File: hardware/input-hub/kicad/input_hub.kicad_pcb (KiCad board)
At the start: 2 copper layers, 116 x 36 mm, 34 parts, among them J1 ACJMIH, J10 XIAO_BAT_SOLDER_ACCESS, J11 S2B-PH-SM4-TB_LF__SN_, J12 PJ-307, J13 PJ-307, J14 PJ-307, J2 ACJMIH, J3 ACJMIH, J5 54602-908LF, J6 BM04B-SRSS-TB_LF__SN_, J7 Conn_01x04, J8 Conn_01x02, U1 102010448, U2 TPD4E05U06DQAR, U3 TPD4E05U06DQAR

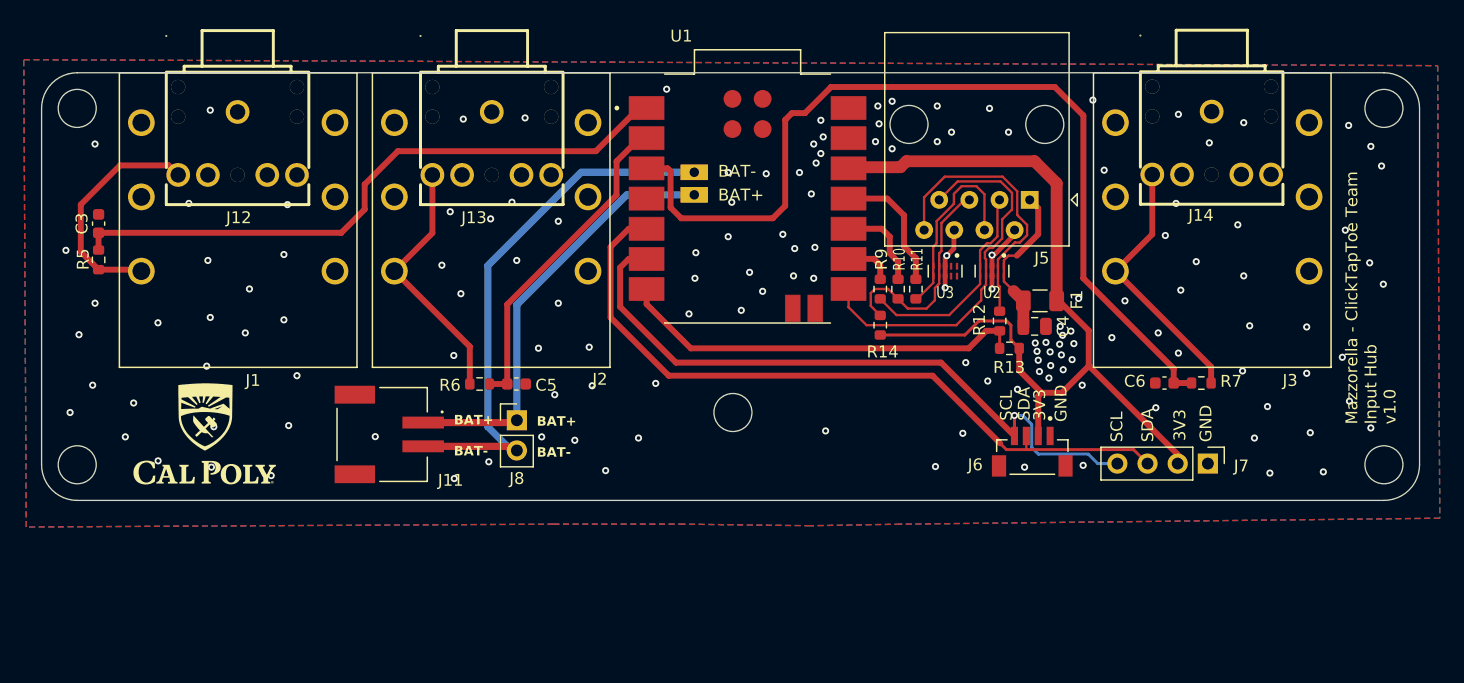
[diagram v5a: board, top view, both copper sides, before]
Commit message: feat: remove third TS jack and make vertical JST battery connector
- Remove the third pedal jack option to reduce board width.
  - Align edge connectors for a cleaner enclosure-facing layout.
  - Replace the horizontal battery JST with a vertical B2B-PH-SM4-TB footprint.
  - Remove stale horizontal JST symbol, footprint, and model assets.
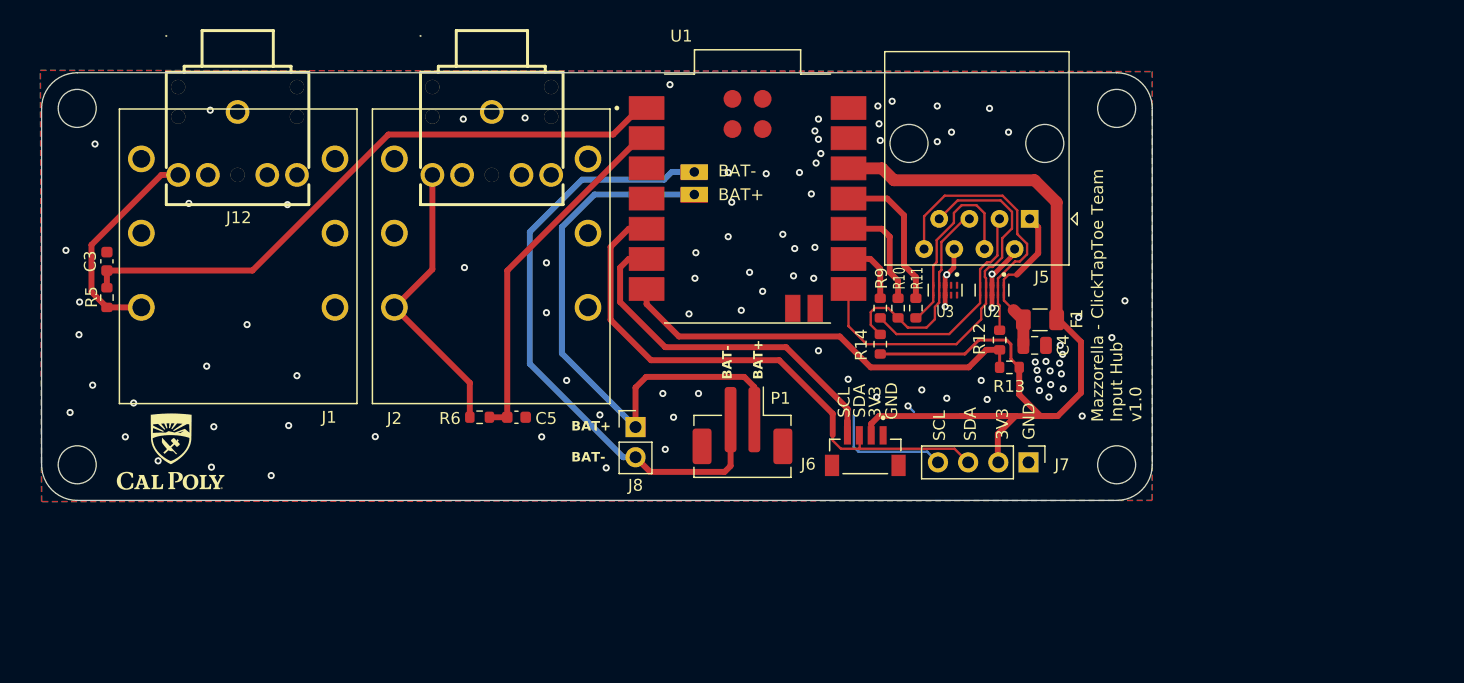
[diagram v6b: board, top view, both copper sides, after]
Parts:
- removed C6: 1u, Capacitor_SMD:C_0603_1608Metric
- removed H5: MountingHole, MountingHole:MountingHole_3.2mm_M3_ISO14580
- removed J10: XIAO_BAT_SOLDER_ACCESS, input_hub:XIAO_BAT_SOLDER_ACCESS
- removed J11: S2B-PH-SM4-TB_LF__SN_, input_hub:JST_S2B-PH-SM4-TB_LF__SN_
- removed J14: PJ-307, input_hub:AUDIO-TH_PJ-307
- removed J3: ACJMIH, input_hub:AMPHENOL_ACJMIH
- removed R7: 330, Resistor_SMD:R_0603_1608Metric
- added J9: XIAO_BAT_SOLDER_ACCESS, input_hub:XIAO_BAT_SOLDER_ACCESS, F.Cu at (151.9, 65.3)
- added P1: B2B-PH-SM4-TB, input_hub:JST_PH_B2B-PH-SM4-TB_1x02-1MP_P2.00mm_Vertical, F.Cu at (156.0, 86.7)
- moved H2 22.5 mm to (187.5, 60.0)
- moved H4 22.5 mm to (187.5, 90.0)
- moved J7 15.1 mm to (180.1, 89.8)
- moved J6 14.1 mm to (166.3, 89.3)
- moved J8 10.0 mm to (147.0, 86.8)
- moved C3 3.25 mm to (102.5, 72.9)
- moved R5 3.25 mm to (102.5, 75.9)
- moved J1 3.05 mm to (113.5, 70.5)
- moved J2 3.05 mm to (134.8, 70.5)
- moved C5 2.80 mm to (137.0, 86.0)
- moved R6 2.80 mm to (133.9, 86.0)
- moved C4 1.60 mm to (180.6, 80.0)
- moved R10 1.60 mm to (169.1, 76.8)
- moved R11 1.60 mm to (170.6, 76.8)
- moved R9 1.60 mm to (167.6, 76.8)
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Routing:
- net Button3: track 77.3 -> 0.00 mm
- net Net-(J14-Pad5): track 22.2 -> 0.00 mm
- net ENC_A: track 61.7 -> 47.3 mm
- net ENC_B: track 56.7 -> 42.9 mm
- net BAT+: track 36.4 -> 48.5 mm
- net +3V3: track 74.1 -> 84.9 mm
- net BAT-: track 45.5 -> 51.8 mm
- net Net-(J13-Pad5): track 21.6 -> 24.5 mm
- net Button2: track 27.4 -> 30.2 mm
- net MOT_RJ45: track 31.8 -> 33.4 mm
- net Net-(U1-D9/MISO): track 7.62 -> 9.22 mm
- net Net-(U1-D10/MOSI): track 11.1 -> 12.7 mm
- net Net-(U1-D8/SCK): track 4.07 -> 5.50 mm
- net Net-(J1-PadT): track 19.6 -> 18.4 mm
- net Net-(U1-D6/TX): track 34.6 -> 35.3 mm
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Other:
- board size 116 x 36 mm -> 93.5 x 36 mm

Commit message: feat: prep input hub for JLC assembly
- Add JLC-oriented board constraints, DRC exclusions, revised vias, and production metadata.
  - Add input hub 3D model links, silkscreen logos, PJ-307 footprint updates, and vertical battery
  JST metadata.
  - Route/document PMW3610 reset and MOTION pull-up support with firmware retry configuration.
  - Clean up remaining EC11 encoder library artifacts and stale encoder nets.
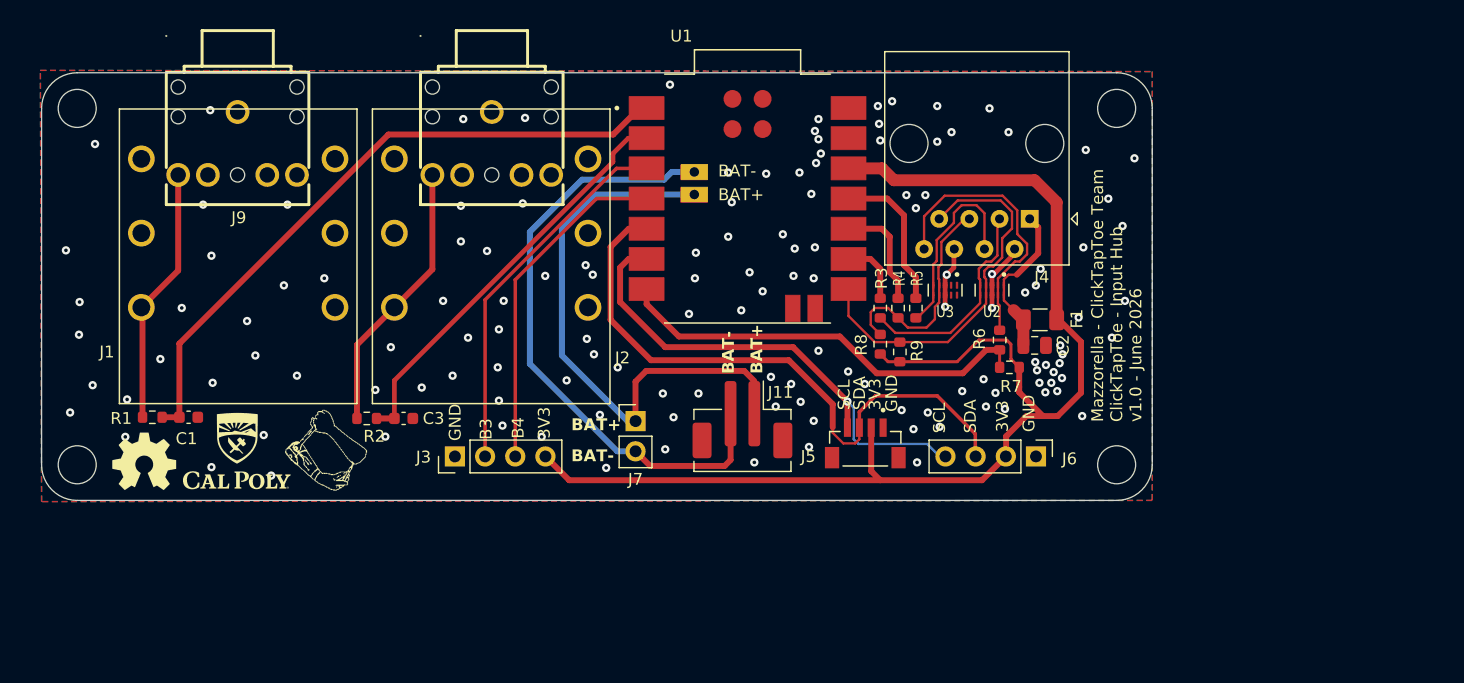
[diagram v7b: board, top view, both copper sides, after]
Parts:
- added G***: EMPOWER_Hand_Line_Silkscreen_7mm_MildSmooth_Mirrored, input_hub:EMPOWER_Hand_Line_Silkscreen_7mm_MildSmooth_Mirrored, F.Cu at (121.0, 88.8)
- added G***: EMPOWER_Hand_Line_Silkscreen_7mm_MildSmooth, input_hub:EMPOWER_Hand_Line_Silkscreen_7mm_MildSmooth, B.Cu at (121.0, 88.8)
- added J3: Conn_01x04, Connector_PinHeader_2.54mm:PinHeader_1x04_P2.54mm_Vertical, F.Cu at (131.8, 89.3)
- added R9: 10k, Resistor_SMD:R_0603_1608Metric, F.Cu at (169.2, 80.5)
- moved C1 14.8 mm to (109.4, 86.0), turned to 180 degrees
- moved R1 10.8 mm to (106.3, 86.0), turned to 180 degrees
- moved C3 9.50 mm to (127.5, 86.1)
- moved R2 9.50 mm to (124.4, 86.1)
- moved J6 0.80 mm to (180.7, 89.3)
- moved J5 0.65 mm to (166.3, 88.7)
- moved J11 0.50 mm to (156.0, 86.2)
- moved J7 0.50 mm to (147.0, 86.3)
- renumbered C3 to C1, C4 to C2, C5 to C3, J13 to J10, P1 to J11, J5 to J4, J6 to J5, J7 to J6, J8 to J7, J9 to J8, J12 to J9, R5 to R1, R6 to R2, R9 to R3, R10 to R4, R11 to R5, R12 to R6, R13 to R7, R14 to R8
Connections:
- net ENC_A renamed SDA
- net ENC_B renamed SCL
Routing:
- net Button3: track 0.00 -> 31.4 mm
- net Button4: track 0.00 -> 28.8 mm
- net +3V3: track 84.9 -> 110.4 mm
- net SDA: track 47.3 -> 52.5 mm
- net Button2: track 30.2 -> 34.8 mm
- net Net-(J1-PadT): track 18.4 -> 21.7 mm
- net Button1: track 52.5 -> 55.2 mm
- net SCL: track 42.9 -> 41.3 mm
- net Net-(J10-Pad5): track 24.5 -> 23.3 mm
- net MOT_RJ45: track 33.4 -> 32.3 mm
- net GND: vias 93 -> 139
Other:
- board text added: "B3"
- board text added: "B4"
- board text added: "Mazzorella - ClickTapToe Team ClickTapToe - Input Hub v1.0 - June 2026"
- board text removed: "Mazzorella - ClickTapToe Team Input Hub v1.0"

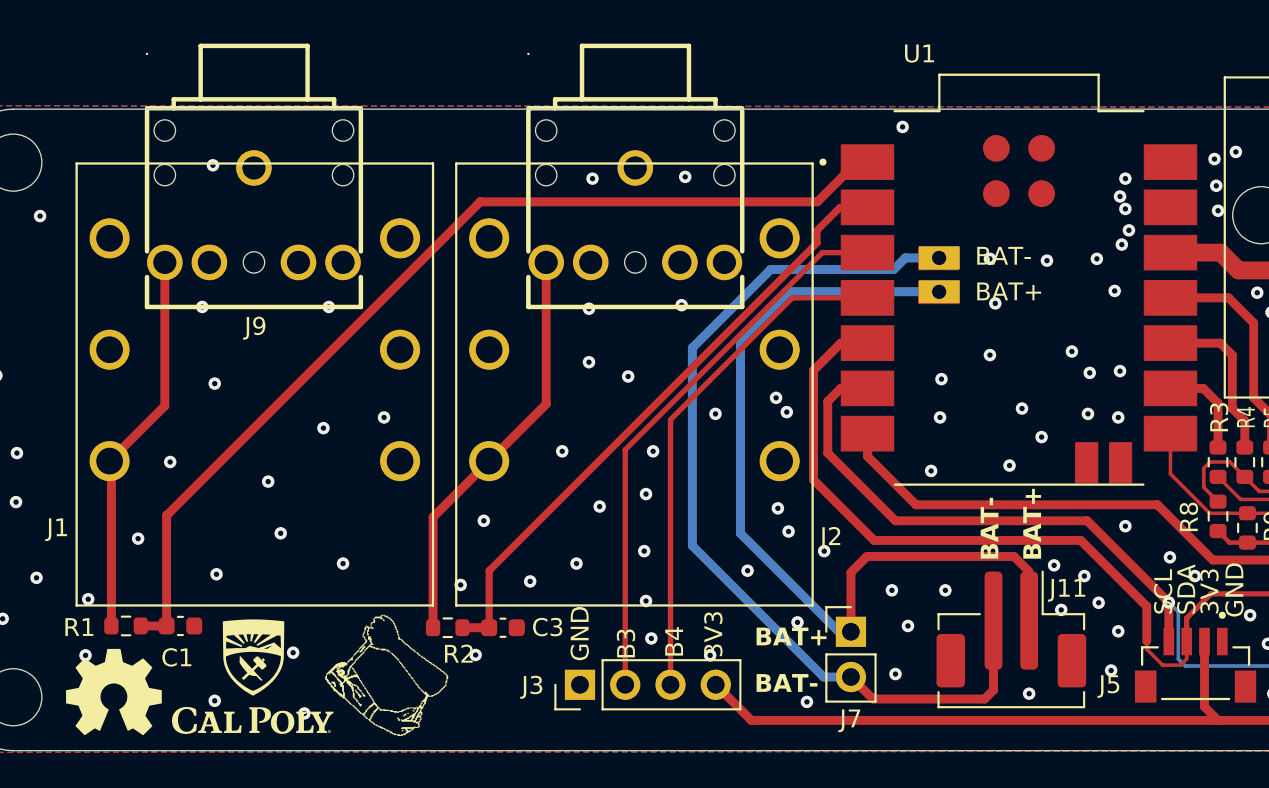
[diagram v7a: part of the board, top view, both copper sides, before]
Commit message: fix: add input hub pedal normal jumpers
- Route pedal jack normal contacts
  through optional 0R jumpers to ground.
  - Use existing 0603 0R jumper sourcing for the new input hub build options.
  - Track release-ready input hub fabrication outputs for ordering.
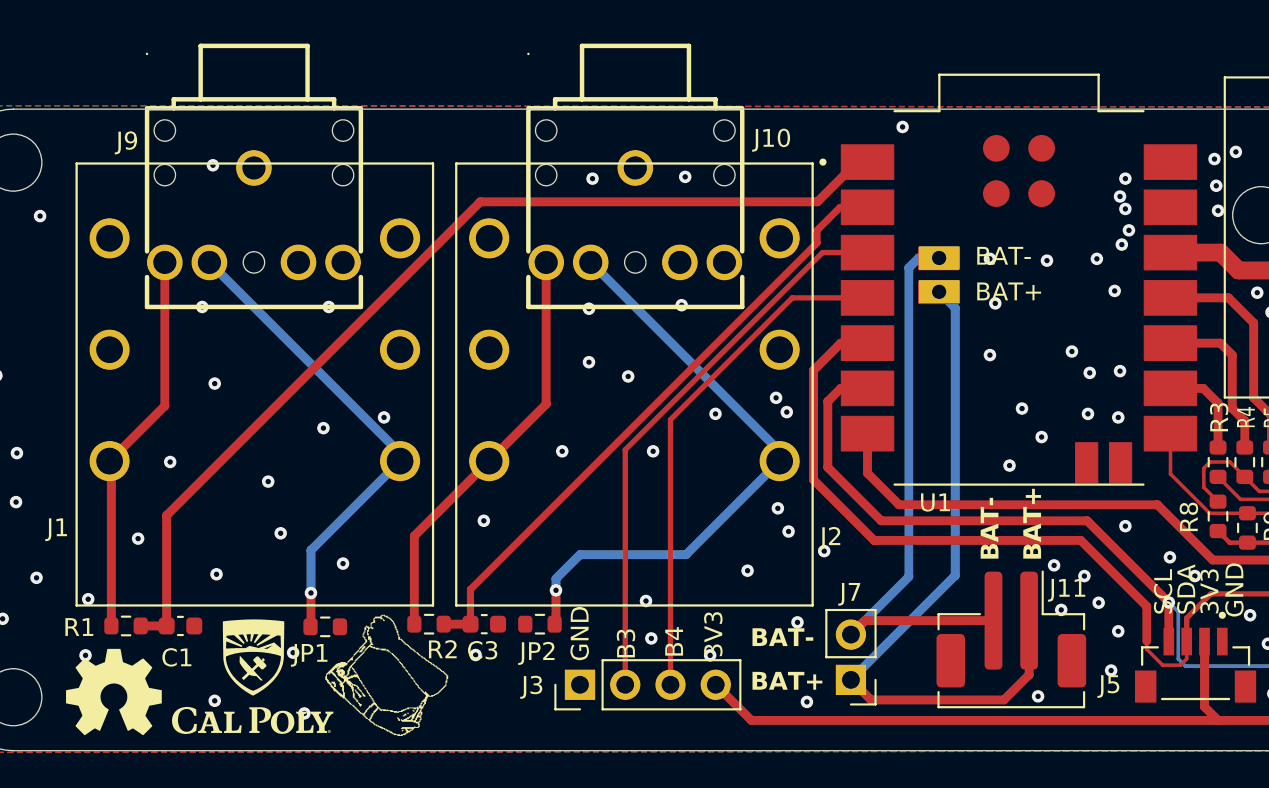
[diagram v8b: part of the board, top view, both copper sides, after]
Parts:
- added JP1: 0R, Resistor_SMD:R_0603_1608Metric, F.Cu at (117.5, 86.0)
- added JP2: 0R, Resistor_SMD:R_0603_1608Metric, F.Cu at (129.6, 85.9)
- moved J7 2.70 mm to (147.0, 89.0), turned to 180 degrees
- moved C3 1.07 mm to (126.4, 85.9)
- moved R2 1.07 mm to (123.3, 85.9)
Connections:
- J1 pad TN: unconnected-(J1-PadTN) -> Net-(J1-PadTN)
- J10 pad 4: unconnected-(J10-Pad4) -> Net-(J10-Pad4)
- J2 pad TN: unconnected-(J2-PadTN) -> Net-(J10-Pad4)
- J9 pad 4: unconnected-(J9-Pad4) -> Net-(J1-PadTN)
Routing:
- net Net-(J10-Pad4): track 0.00 -> 33.4 mm, vias 0 -> 1
- net Net-(J1-PadTN): track 0.00 -> 27.1 mm, vias 0 -> 1
- net BAT-: track 51.6 -> 32.2 mm
- net BAT+: track 48.4 -> 41.4 mm
- net Net-(U1-D6/TX): track 35.7 -> 36.3 mm
- net GND: vias 139 -> 126
